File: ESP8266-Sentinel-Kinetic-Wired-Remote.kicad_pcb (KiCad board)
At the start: 2 copper layers, 80 x 48.8 mm, 46 parts, among them J1 Conn_01x04_Socket, J2 Screw_Terminal_01x04, J3 Conn_01x06_Pin, Q1 AO3400A, SW1 SW_Push, SW2 SW_Push, SW3 SW_Push, SW4 SW_Push, SW5 SW_Push, U1 AMS1117-3.3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

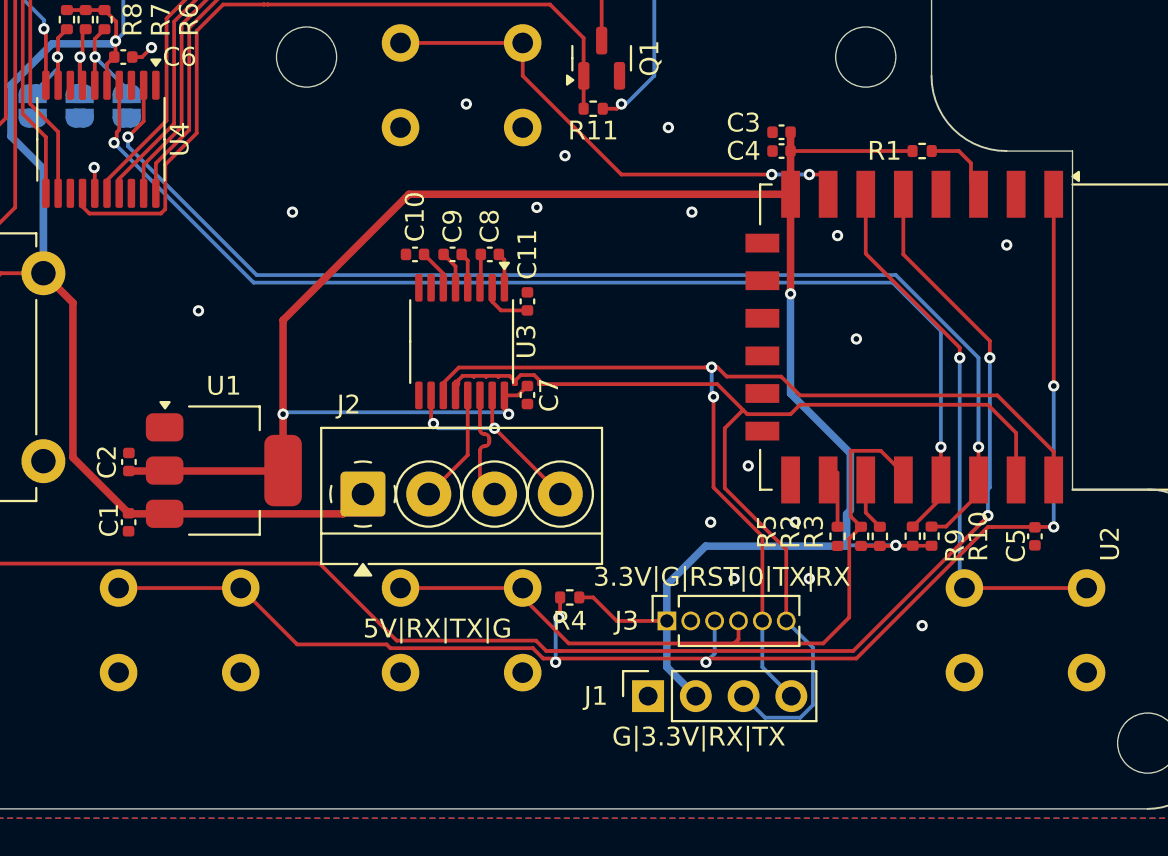
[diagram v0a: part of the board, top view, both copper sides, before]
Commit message: Added JLCPCB part numbers Rotated programming ports
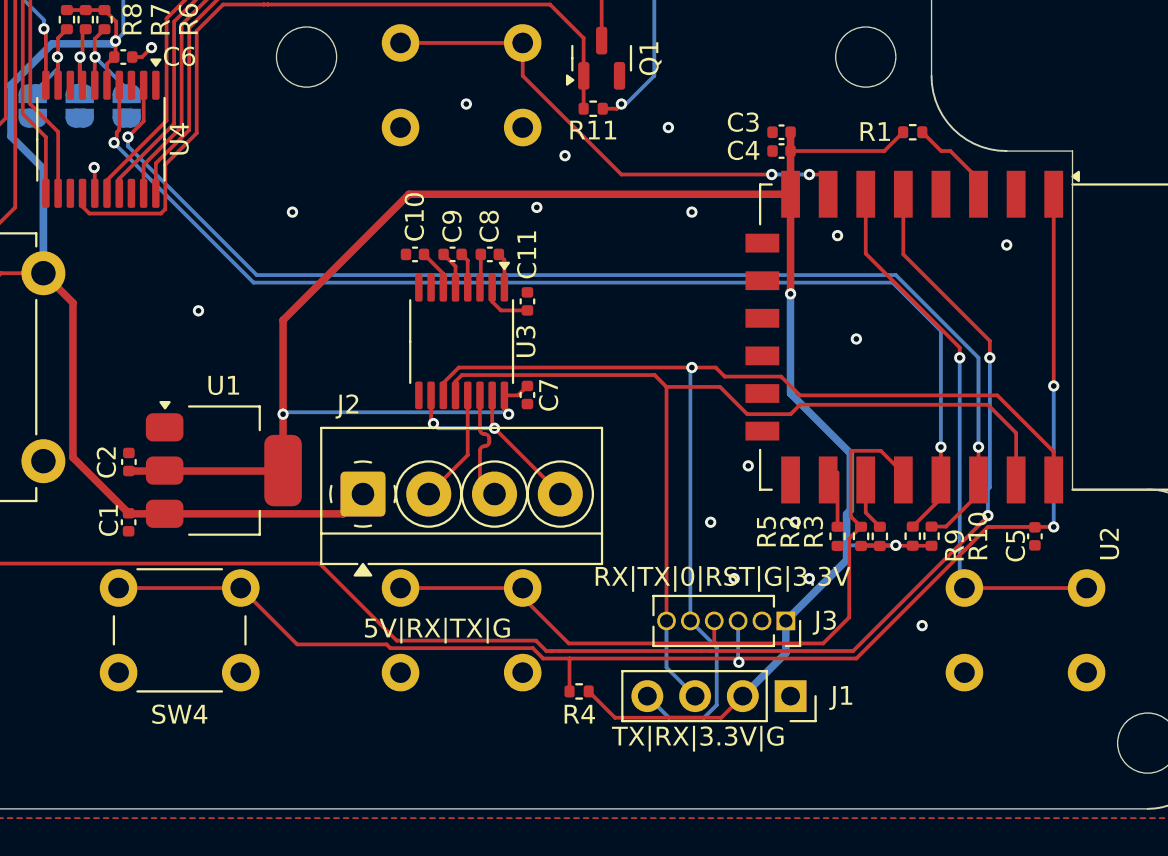
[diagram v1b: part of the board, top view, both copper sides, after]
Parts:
- Q1: value AO3400A -> SS8050
- SW4: moved to F.Cu
- moved J1 7.58 mm to (167.5, 132.5), turned to -90 degrees
- moved SW4 6.50 mm to (131.8, 126.8), turned to 0 degrees
- moved J3 6.33 mm to (167.2, 128.5), turned to -90 degrees
- moved R4 5.02 mm to (156.2, 132.2)
- moved R1 1.12 mm to (174.0, 102.5)
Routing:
- net /RX: track 58.5 -> 52.0 mm
- net /TX: track 55.2 -> 58.9 mm, vias 2 -> 1
- net +3.3V: track 118.9 -> 116.3 mm
- net /RST: track 78.7 -> 76.8 mm, vias 5 -> 3
- net Net-(U2-EN): track 3.26 -> 3.91 mm
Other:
- board text added: "RX|TX|0|RST|G|3.3V"
- board text added: "TX|RX|3.3V|G"
- board text removed: "3.3V|G|RST|0|TX|RX"
- board text removed: "G|3.3V|RX|TX"

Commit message: Add JLCPCB part number for SS8050 Remove panel creation action
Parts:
- RV1, RV2: value 5K -> 10K
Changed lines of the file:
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@@
 			)
 		)
-		(property "Value" "5K"
+		(property "Value" "10K"
 			(at 7.5 3.25 0)
 			(layer "F.Fab")
@@
 			)
 		)
-		(property "Value" "5K"
+		(property "Value" "10K"
 			(at 2.6 7.4 90)
 			(layer "F.Fab")
@@
 		(sheetname "/")
 		(sheetfile "ESP8266-Sentinel-Kinetic-Wired-Remote.kicad_sch")
-		(attr through_hole)
+		(attr through_hole exclude_from_bom)
 		(fp_line
 			(start 1.99 5.81)
@@
 		(sheetname "/")
 		(sheetfile "ESP8266-Sentinel-Kinetic-Wired-Remote.kicad_sch")
-		(attr through_hole)
+		(attr through_hole exclude_from_bom)
 		(fp_line
 			(start -0.25 1.5)
@@
 			)
 		)
+		(property "LCSC" "C2150"
+			(at 0 0 90)
+			(unlocked yes)
+			(layer "F.Fab")
+			(hide yes)
+			(effects
+				(font
+					(size 1 1)
+					(thickness 0.15)
+				)
+			)
+		)
 		(property ki_fp_filters "SOT?23*")
 		(sheetname "/")
@@
 		(sheetname "/")
 		(sheetfile "ESP8266-Sentinel-Kinetic-Wired-Remote.kicad_sch")
-		(attr through_hole)
+		(attr through_hole exclude_from_bom)
 		(fp_line
 			(start -2.22 -3.52)
@@
 		(sheetname "/")
 		(sheetfile "ESP8266-Sentinel-Kinetic-Wired-Remote.kicad_sch")
-		(attr through_hole)
+		(attr through_hole exclude_from_bom)
 		(fp_line
 			(start 6.75 -3)
@@
 		(sheetname "/")
 		(sheetfile "ESP8266-Sentinel-Kinetic-Wired-Remote.kicad_sch")
-		(attr through_hole)
+		(attr through_hole exclude_from_bom)
 		(fp_line
 			(start 6.75 -3)
@@
 		(sheetname "/")
 		(sheetfile "ESP8266-Sentinel-Kinetic-Wired-Remote.kicad_sch")
-		(attr through_hole)
+		(attr through_hole exclude_from_bom)
 		(fp_line
 			(start 6.75 -3)
@@
 		(sheetname "/")
 		(sheetfile "ESP8266-Sentinel-Kinetic-Wired-Remote.kicad_sch")
-		(attr through_hole)
+		(attr through_hole exclude_from_bom)
 		(fp_line
 			(start 6.75 -3)
@@
 		(sheetname "/")
 		(sheetfile "ESP8266-Sentinel-Kinetic-Wired-Remote.kicad_sch")
-		(attr through_hole)
+		(attr through_hole exclude_from_bom)
 		(fp_line
 			(start -8.14 -33.64)

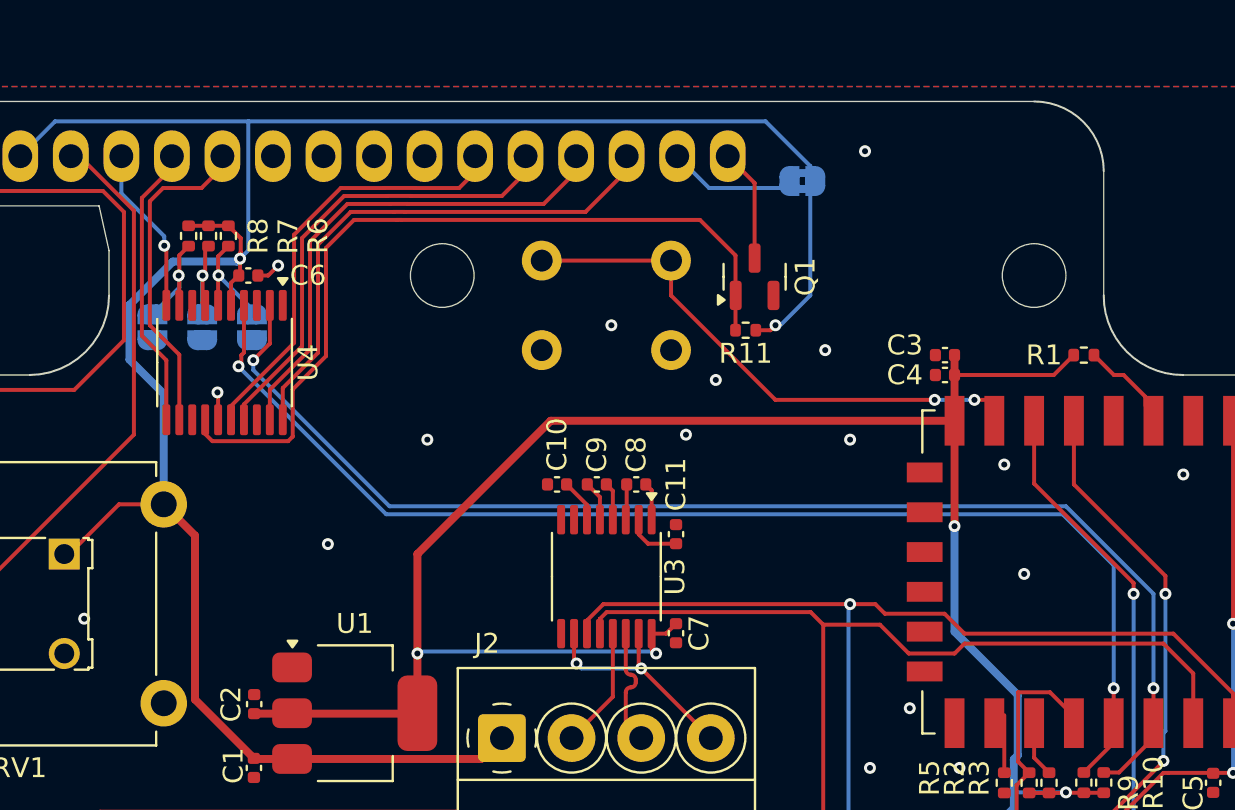
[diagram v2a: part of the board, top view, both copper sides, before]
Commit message: Replaced PCF8574 package
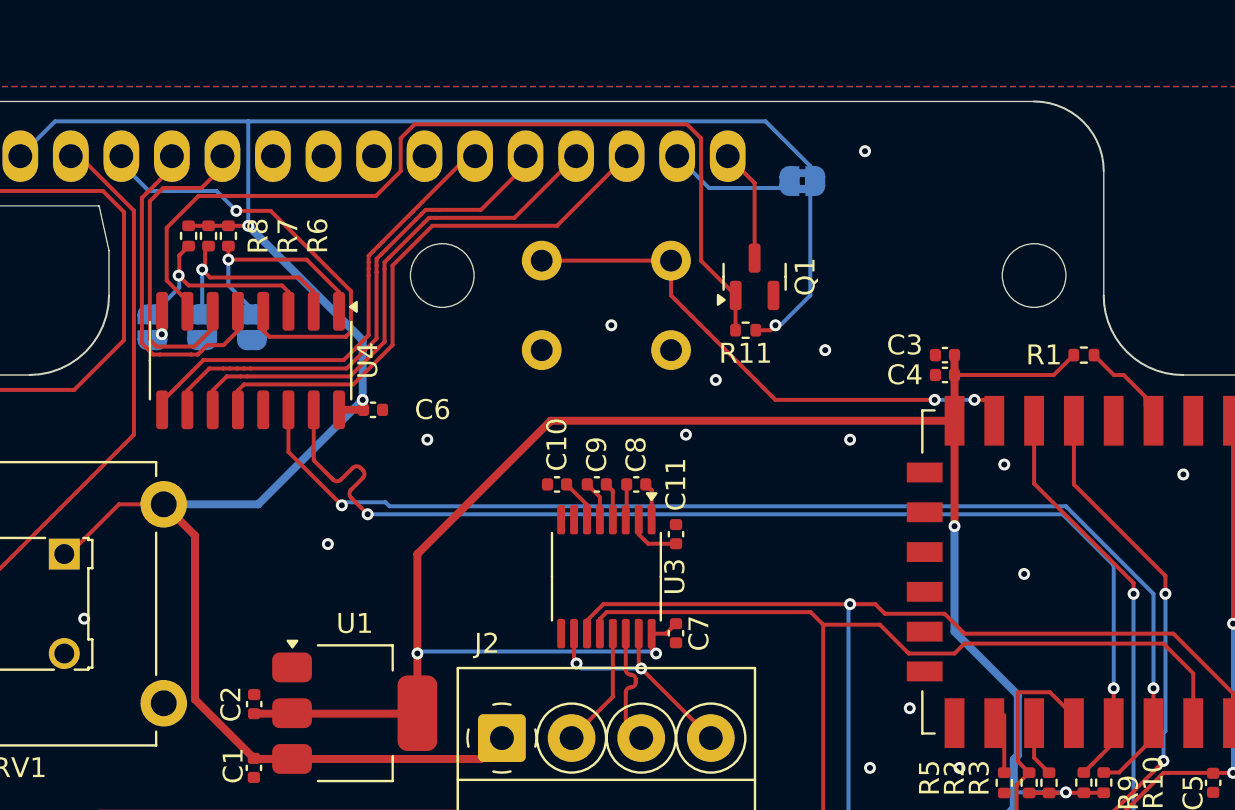
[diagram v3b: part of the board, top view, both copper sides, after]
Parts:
- U4: value PCF8574TS -> PCF8574T; footprint Package_SO:SSOP-20_4.4x6.5mm_P0.65mm -> Package_SO:SOIC-16_3.9x9.9mm_P1.27mm
- moved C6 9.21 mm to (138.3, 105.2)
- moved U4 1.31 mm to (132.1, 102.8)
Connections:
- U4 pad 1: unconnected-(U4-~{INT}-Pad1) -> Net-(JP3-B)
- U4 pad 10: Net-(DS1-RS) -> Net-(DS1-D5)
- U4 pad 11: Net-(DS1-R/W) -> Net-(DS1-D6)
- U4 pad 12: Net-(DS1-E) -> Net-(DS1-D7)
- U4 pad 14: Net-(Q1-B) -> /SCL
- U4 pad 15: GND -> /SDA
- U4 pad 16: Net-(DS1-D4) -> +5V
- U4 pad 2: /SCL -> Net-(JP1-B)
- U4 pad 3: unconnected-(U4-NC-Pad3) -> Net-(JP2-B)
- U4 pad 4: /SDA -> Net-(DS1-RS)
- U4 pad 5: +5V -> Net-(DS1-R/W)
- U4 pad 6: Net-(JP3-B) -> Net-(DS1-E)
- U4 pad 7: Net-(JP1-B) -> Net-(Q1-B)
- U4 pad 8: unconnected-(U4-NC-Pad8) -> GND
- U4 pad 9: Net-(JP2-B) -> Net-(DS1-D4)
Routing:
- net Net-(DS1-RS): track 8.44 -> 22.2 mm
- net Net-(JP1-B): track 4.88 -> 10.4 mm
- net Net-(JP2-B): track 5.72 -> 11.0 mm
- net Net-(JP3-B): track 5.61 -> 10.9 mm
- net /SCL: track 62.3 -> 57.5 mm
- net /SDA: track 60.5 -> 56.3 mm
- net Net-(Q1-B): track 41.2 -> 45.3 mm
- net Net-(DS1-D4): track 21.0 -> 23.6 mm
- net +5V: track 115.4 -> 117.9 mm, vias 2 -> 3
- net Net-(DS1-D5): track 23.0 -> 25.5 mm
- net Net-(DS1-R/W): track 13.8 -> 16.0 mm
- net Net-(DS1-D6): track 24.6 -> 26.5 mm
- net GND: track 43.8 -> 42.4 mm, vias 22 -> 21
- net Net-(DS1-D7): track 26.6 -> 27.7 mm

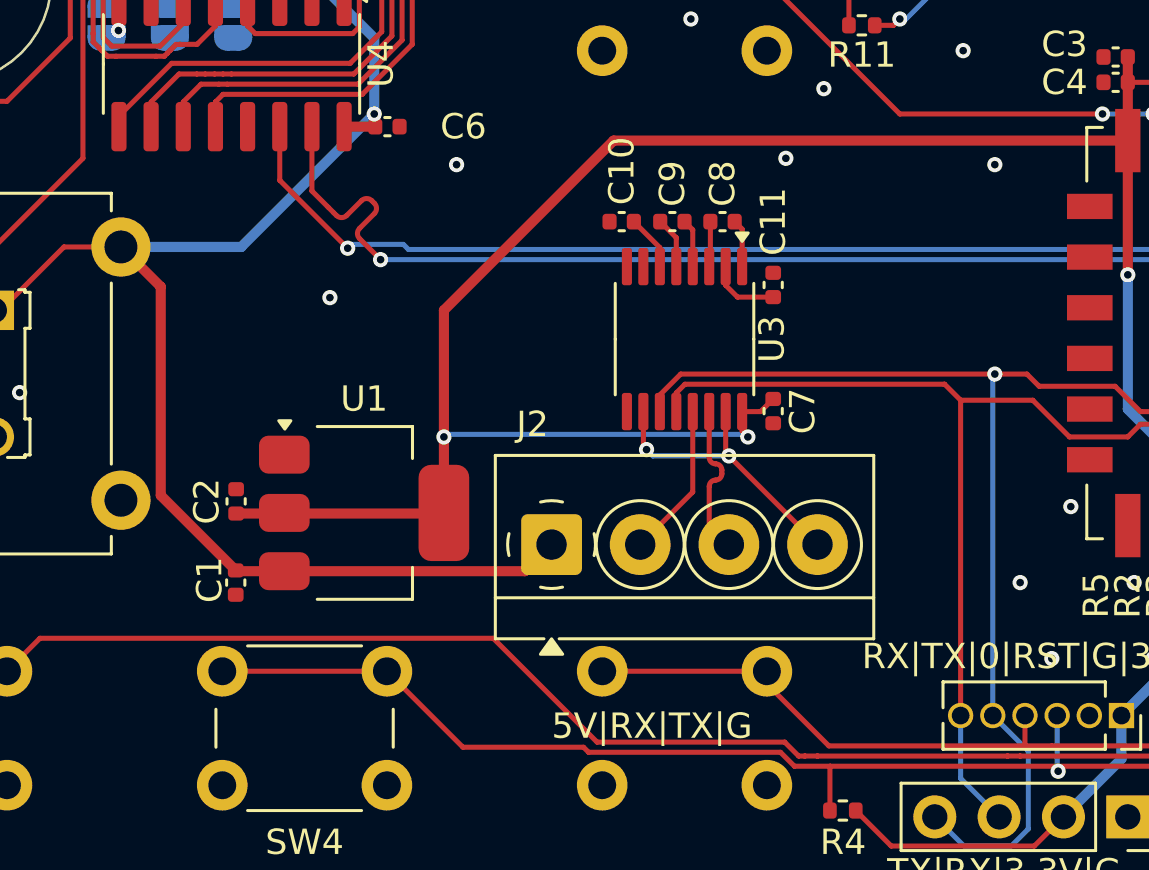
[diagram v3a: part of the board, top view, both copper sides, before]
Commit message: Added TVS diodes for protection
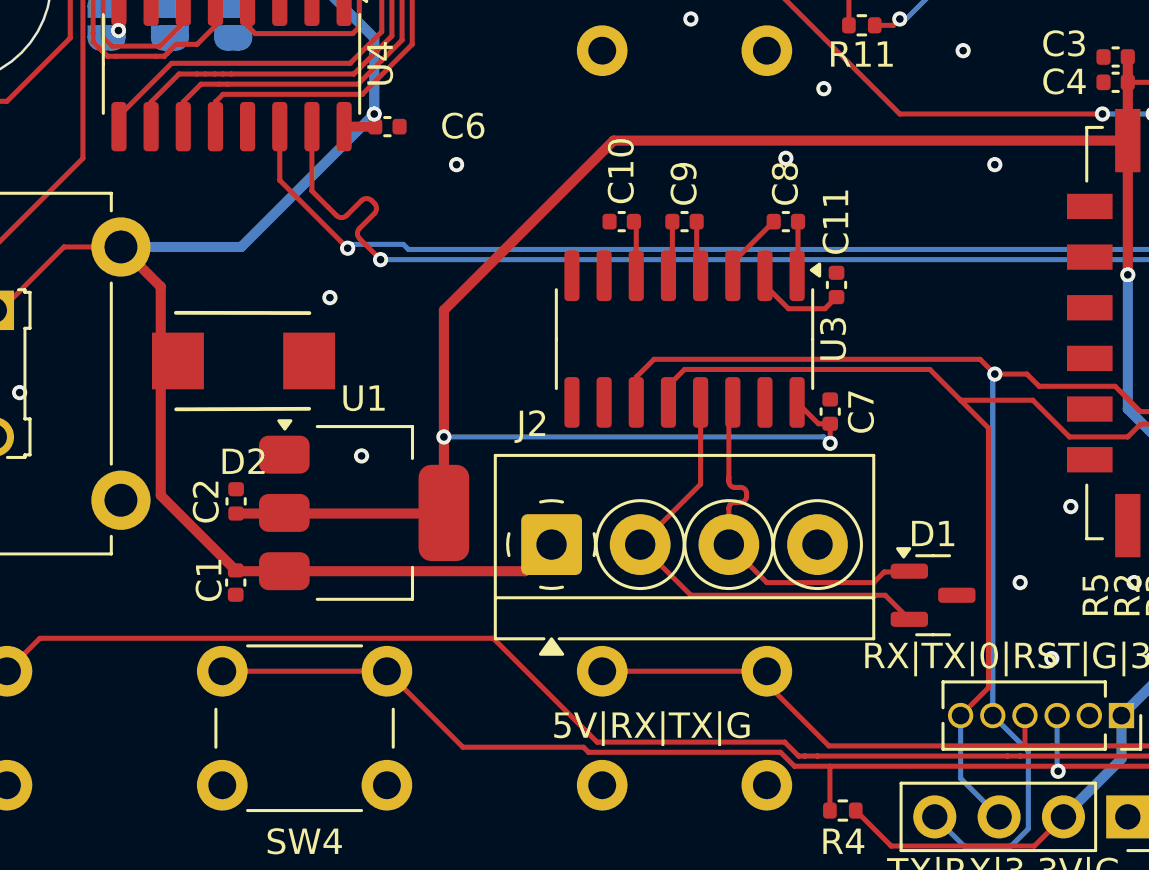
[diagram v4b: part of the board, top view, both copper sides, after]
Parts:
- added D1: PSM712-LF-T7, Package_TO_SOT_SMD:SOT-23, F.Cu at (159.8, 123.8)
- added D2: P6SMB6.8CA-C78395, lib:SMB_L4.6-W3.6-LS5.3-BI, F.Cu at (132.6, 114.5)
- U3: footprint Package_SO:TSSOP-16_4.4x5mm_P0.65mm -> Package_SO:SOP-16_3.9x9.9mm_P1.27mm
- moved C11 2.50 mm to (156.0, 111.5)
- moved C8 2.50 mm to (154.0, 109.0)
- moved C7 2.25 mm to (155.8, 116.5), turned to 90 degrees
- moved C9 0.48 mm to (150.0, 109.0)
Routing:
- net /RS232_RX: track 6.11 -> 18.4 mm
- net GND: track 42.4 -> 30.7 mm, vias 21 -> 20
- net /RS232_TX: track 5.01 -> 14.6 mm
- net +3.3V: track 116.3 -> 119.5 mm
- net /RX: track 52.0 -> 53.5 mm
- net /TX: track 58.9 -> 60.4 mm
- net Net-(U3-C1-): track 1.73 -> 2.81 mm
- net Net-(U3-VS+): track 2.81 -> 3.77 mm
